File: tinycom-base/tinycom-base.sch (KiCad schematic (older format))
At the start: 34 parts, among them J1 MICRO_SD_HINGE, P1 CONN_02X08, P2 CONN_02X08, P3 USB_A, P4 USB_OTG, U1 SY8008BAAC, U2 SY8008BAAC, U3 SY8008BAAC

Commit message: rename wifi->basse
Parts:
- removed R10, R11, R12, R8, R9: R_Small, Resistors_SMD:R_0805, symbol R_Small
- added HDMI1: HDMI-SWM-19, tinycom:HDMI-SWM-19, symbol HDMI-SWM-19
- added U4: RTL8723BS(ComboModule), tinycom:RL-SM02BD(RTL8723BS), symbol RTL8723BS(ComboModule)
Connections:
- wire segments 124 -> 118
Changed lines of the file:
@@
 LIBS:stm32-48pin-devBoard
 LIBS:OPL-Inductor
-LIBS:tinycom-base-cache
+LIBS:tinycom
+LIBS:hdmi-swm-19
+LIBS:tinycom-wifi-cache
 EELAYER 25 0
 EELAYER END
@@
 $EndComp
 $Comp
-L MICRO_SD_HINGE J1
-U 1 1 562BAACC
-P 8950 4450
-F 0 "J1" H 9000 4500 60  0000 C CNN
-F 1 "MICRO_SD_HINGE" H 8950 5000 60  0000 C CNN
-F 2 "armory:MICRO_SD_HINGE_AMP" V 9060 3950 60  0001 C CNN
-F 3 "" V 9060 3950 60  0000 C CNN
-	1    8950 4450
-	1    0    0    -1
-$EndComp
-$Comp
 L SY8008BAAC U1
 U 1 1 562D9C58
@@
 $EndComp
 $Comp
-L +5V #PWR01
+L +5V #PWR14
 U 1 1 562DA8F7
 P 5250 4200
-F 0 "#PWR01" H 5250 4050 50  0001 C CNN
+F 0 "#PWR14" H 5250 4050 50  0001 C CNN
 F 1 "+5V" H 5250 4340 50  0000 C CNN
 F 2 "" H 5250 4200 60  0000 C CNN
@@
 $EndComp
 $Comp
-L GND #PWR02
+L GND #PWR15
 U 1 1 562DA928
 P 5250 4600
-F 0 "#PWR02" H 5250 4350 50  0001 C CNN
+F 0 "#PWR15" H 5250 4350 50  0001 C CNN
 F 1 "GND" H 5250 4450 50  0000 C CNN
 F 2 "" H 5250 4600 60  0000 C CNN
@@
 UDP0
 $Comp
-L +5V #PWR03
+L +5V #PWR16
 U 1 1 562DAC42
 P 5300 5050
-F 0 "#PWR03" H 5300 4900 50  0001 C CNN
+F 0 "#PWR16" H 5300 4900 50  0001 C CNN
 F 1 "+5V" H 5300 5190 50  0000 C CNN
 F 2 "" H 5300 5050 60  0000 C CNN
@@
 $EndComp
 $Comp
-L GND #PWR04
+L GND #PWR17
 U 1 1 562DAC77
 P 5300 5500
-F 0 "#PWR04" H 5300 5250 50  0001 C CNN
+F 0 "#PWR17" H 5300 5250 50  0001 C CNN
 F 1 "GND" H 5300 5350 50  0000 C CNN
 F 2 "" H 5300 5500 60  0000 C CNN
@@
 UDP1
 $Comp
-L GND #PWR05
+L GND #PWR5
 U 1 1 562DAF0B
 P 1350 1750
-F 0 "#PWR05" H 1350 1500 50  0001 C CNN
+F 0 "#PWR5" H 1350 1500 50  0001 C CNN
 F 1 "GND" H 1350 1600 50  0000 C CNN
 F 2 "" H 1350 1750 60  0000 C CNN
@@
 $EndComp
 $Comp
-L +5V #PWR06
+L +5V #PWR3
 U 1 1 562DAF87
 P 1250 1350
-F 0 "#PWR06" H 1250 1200 50  0001 C CNN
+F 0 "#PWR3" H 1250 1200 50  0001 C CNN
 F 1 "+5V" H 1250 1490 50  0000 C CNN
 F 2 "" H 1250 1350 60  0000 C CNN
@@
 $EndComp
 $Comp
-L +5V #PWR07
+L +5V #PWR1
 U 1 1 562DB0A5
 P 1150 2550
-F 0 "#PWR07" H 1150 2400 50  0001 C CNN
+F 0 "#PWR1" H 1150 2400 50  0001 C CNN
 F 1 "+5V" H 1150 2690 50  0000 C CNN
 F 2 "" H 1150 2550 60  0000 C CNN
@@
 $EndComp
 $Comp
-L GND #PWR08
+L GND #PWR6
 U 1 1 562DB1B7
 P 1350 2900
-F 0 "#PWR08" H 1350 2650 50  0001 C CNN
+F 0 "#PWR6" H 1350 2650 50  0001 C CNN
 F 1 "GND" H 1350 2750 50  0000 C CNN
 F 2 "" H 1350 2900 60  0000 C CNN
@@
 $EndComp
 $Comp
-L +5V #PWR09
+L +5V #PWR2
 U 1 1 562DB2B7
 P 1150 3800
-F 0 "#PWR09" H 1150 3650 50  0001 C CNN
+F 0 "#PWR2" H 1150 3650 50  0001 C CNN
 F 1 "+5V" H 1150 3940 50  0000 C CNN
 F 2 "" H 1150 3800 60  0000 C CNN
@@
 $EndComp
 $Comp
-L GND #PWR010
+L GND #PWR4
 U 1 1 562DB346
 P 1300 4150
-F 0 "#PWR010" H 1300 3900 50  0001 C CNN
+F 0 "#PWR4" H 1300 3900 50  0001 C CNN
 F 1 "GND" H 1300 4000 50  0000 C CNN
 F 2 "" H 1300 4150 60  0000 C CNN
@@
 VCC_15
 $Comp
-L GND #PWR011
+L GND #PWR19
 U 1 1 562DAEC4
 P 7450 2400
-F 0 "#PWR011" H 7450 2150 50  0001 C CNN
+F 0 "#PWR19" H 7450 2150 50  0001 C CNN
 F 1 "GND" H 7450 2250 50  0000 C CNN
 F 2 "" H 7450 2400 60  0000 C CNN
@@
 $EndComp
 $Comp
-L GND #PWR012
+L GND #PWR21
 U 1 1 562DA997
 P 8650 2450
-F 0 "#PWR012" H 8650 2200 50  0001 C CNN
+F 0 "#PWR21" H 8650 2200 50  0001 C CNN
 F 1 "GND" H 8650 2300 50  0000 C CNN
 F 2 "" H 8650 2450 60  0000 C CNN
@@
 SDC0_D1
 $Comp
-L GND #PWR013
+L GND #PWR20
 U 1 1 562DAEE9
 P 7450 4950
-F 0 "#PWR013" H 7450 4700 50  0001 C CNN
+F 0 "#PWR20" H 7450 4700 50  0001 C CNN
 F 1 "GND" H 7450 4800 50  0000 C CNN
 F 2 "" H 7450 4950 60  0000 C CNN
@@
 $EndComp
 $Comp
-L GND #PWR014
+L GND #PWR22
 U 1 1 562DAF47
 P 9050 5450
-F 0 "#PWR014" H 9050 5200 50  0001 C CNN
+F 0 "#PWR22" H 9050 5200 50  0001 C CNN
 F 1 "GND" H 9050 5300 50  0000 C CNN
 F 2 "" H 9050 5450 60  0000 C CNN
@@
 $EndComp
 $Comp
-L +3.3V #PWR015
+L +3.3V #PWR18
 U 1 1 562DB369
 P 7300 4000
-F 0 "#PWR015" H 7300 3850 50  0001 C CNN
+F 0 "#PWR18" H 7300 3850 50  0001 C CNN
 F 1 "+3.3V" H 7300 4140 50  0000 C CNN
 F 2 "" H 7300 4000 60  0000 C CNN
@@
 $EndComp
 $Comp
-L GND #PWR016
+L GND #PWR9
 U 1 1 562DB89F
 P 3250 2000
-F 0 "#PWR016" H 3250 1750 50  0001 C CNN
+F 0 "#PWR9" H 3250 1750 50  0001 C CNN
 F 1 "GND" H 3250 1850 50  0000 C CNN
 F 2 "" H 3250 2000 60  0000 C CNN
@@
 $EndComp
 $Comp
-L +3.3V #PWR017
+L +3.3V #PWR10
 U 1 1 562DBC47
 P 3600 1350
-F 0 "#PWR017" H 3600 1200 50  0001 C CNN
+F 0 "#PWR10" H 3600 1200 50  0001 C CNN
 F 1 "+3.3V" H 3600 1490 50  0000 C CNN
 F 2 "" H 3600 1350 60  0000 C CNN
@@
 $EndComp
 $Comp
-L GND #PWR018
+L GND #PWR8
 U 1 1 562F8BF0
 P 3150 3150
-F 0 "#PWR018" H 3150 2900 50  0001 C CNN
+F 0 "#PWR8" H 3150 2900 50  0001 C CNN
 F 1 "GND" H 3150 3000 50  0000 C CNN
 F 2 "" H 3150 3150 60  0000 C CNN
@@
 $EndComp
 $Comp
-L GND #PWR019
+L GND #PWR7
 U 1 1 562F9FD4
 P 3100 4550
-F 0 "#PWR019" H 3100 4300 50  0001 C CNN
+F 0 "#PWR7" H 3100 4300 50  0001 C CNN
 F 1 "GND" H 3100 4400 50  0000 C CNN
 F 2 "" H 3100 4550 60  0000 C CNN
@@
 $EndComp
 $Comp
-L GND #PWR020
+L GND #PWR11
 U 1 1 56336272
 P 4400 1900
-F 0 "#PWR020" H 4400 1650 50  0001 C CNN
+F 0 "#PWR11" H 4400 1650 50  0001 C CNN
 F 1 "GND" H 4400 1750 50  0000 C CNN
 F 2 "" H 4400 1900 60  0000 C CNN
@@
 $EndComp
 $Comp
-L +3.3V #PWR021
-U 1 1 563494F9
-P 8050 3600
-F 0 "#PWR021" H 8050 3450 50  0001 C CNN
-F 1 "+3.3V" H 8050 3740 50  0000 C CNN
-F 2 "" H 8050 3600 60  0000 C CNN
-F 3 "" H 8050 3600 60  0000 C CNN
-	1    8050 3600
-	1    0    0    -1
-$EndComp
-$Comp
-L R_Small R8
-U 1 1 56349670
-P 7850 3750
-F 0 "R8" H 7880 3770 50  0000 L CNN
-F 1 "R_Small" H 7880 3710 50  0000 L CNN
-F 2 "Resistors_SMD:R_0805" H 7850 3750 60  0001 C CNN
-F 3 "" H 7850 3750 60  0000 C CNN
-	1    7850 3750
-	1    0    0    -1
-$EndComp
-$Comp
-L R_Small R9
-U 1 1 56349787
-P 7950 3750
-F 0 "R9" H 7980 3770 50  0000 L CNN
-F 1 "R_Small" H 7980 3710 50  0000 L CNN
-F 2 "Resistors_SMD:R_0805" H 7950 3750 60  0001 C CNN
-F 3 "" H 7950 3750 60  0000 C CNN
-	1    7950 3750
-	1    0    0    -1
-$EndComp
-$Comp
-L R_Small R10
-U 1 1 56349823
-P 8050 3750
-F 0 "R10" H 8080 3770 50  0000 L CNN
-F 1 "R_Small" H 8080 3710 50  0000 L CNN
-F 2 "Resistors_SMD:R_0805" H 8050 3750 60  0001 C CNN
-F 3 "" H 8050 3750 60  0000 C CNN
-	1    8050 3750
-	1    0    0    -1
-$EndComp
-$Comp
-L R_Small R11
-U 1 1 5634988E
-P 8150 3750
-F 0 "R11" H 8180 3770 50  0000 L CNN
-F 1 "R_Small" H 8180 3710 50  0000 L CNN
-F 2 "Resistors_SMD:R_0805" H 8150 3750 60  0001 C CNN
-F 3 "" H 8150 3750 60  0000 C CNN
-	1    8150 3750
-	1    0    0    -1
-$EndComp
-$Comp
-L R_Small R12
-U 1 1 56349916
-P 8250 3750
-F 0 "R12" H 8280 3770 50  0000 L CNN
-F 1 "R_Small" H 8280 3710 50  0000 L CNN
-F 2 "Resistors_SMD:R_0805" H 8250 3750 60  0001 C CNN
-F 3 "" H 8250 3750 60  0000 C CNN
-	1    8250 3750
-	1    0    0    -1
-$EndComp
-$Comp
 L C_Small C8
 U 1 1 5634A812
@@
 $EndComp
 $Comp
-L GND #PWR022
+L GND #PWR12
 U 1 1 5634B03F
 P 4900 4550
-F 0 "#PWR022" H 4900 4300 50  0001 C CNN
+F 0 "#PWR12" H 4900 4300 50  0001 C CNN
 F 1 "GND" H 4900 4400 50  0000 C CNN
 F 2 "" H 4900 4550 60  0000 C CNN
@@
 $EndComp
 $Comp
-L GND #PWR023
+L GND #PWR13
 U 1 1 5634B0B0
 P 4900 5400
-F 0 "#PWR023" H 4900 5150 50  0001 C CNN
+F 0 "#PWR13" H 4900 5150 50  0001 C CNN
 F 1 "GND" H 4900 5250 50  0000 C CNN
 F 2 "" H 4900 5400 60  0000 C CNN
@@
 	8150 4050 7900 4050
 Wire Wire Line
-	7850 3600 8250 3600
-Wire Wire Line
-	7850 3600 7850 3650
-Wire Wire Line
-	8250 3600 8250 3650
-Connection ~ 8050 3600
-Wire Wire Line
-	7950 3650 7950 3600
-Connection ~ 7950 3600
-Wire Wire Line
-	8050 3650 8050 3600
-Wire Wire Line
-	8150 3650 8150 3600
-Connection ~ 8150 3600
-Wire Wire Line
-	8250 3850 8250 4000
-Wire Wire Line
 	8250 4000 8150 4000
 Wire Wire Line
 	8150 4000 8150 4050
-Wire Wire Line
-	8150 3850 8150 3900
-Wire Wire Line
-	8150 3900 8100 3900
-Wire Wire Line
-	8100 3900 8100 4150
 Connection ~ 8100 4150
-Wire Wire Line
-	8050 3850 8050 4250
 Connection ~ 8050 4250
-Wire Wire Line
-	8000 4650 8000 3850
-Wire Wire Line
-	8000 3850 7950 3850
 Connection ~ 8000 4650
-Wire Wire Line
-	7850 3850 7850 3950
-Wire Wire Line
-	7850 3950 7950 3950
-Wire Wire Line
-	7950 3950 7950 4750
 Connection ~ 7950 4750
 Wire Wire Line
@@
 	5350 4850 5850 4850
 Connection ~ 5350 4650
+$Comp
+L RTL8723BS(ComboModule) U4
+U 1 1 56591901
+P 2000 6200
+F 0 "U4" H 1600 7575 60  0000 C CNN
+F 1 "RTL8723BS(ComboModule)" H 2000 4825 60  0000 C CNN
+F 2 "tinycom:RL-SM02BD(RTL8723BS)" H 2000 6000 60  0000 C CNN
+F 3 "" H 2000 6000 60  0000 C CNN
+	1    2000 6200
+	1    0    0    -1
+$EndComp
+Wire Wire Line
+	7950 3950 7950 4750
+Wire Wire Line
+	7850 3950 7950 3950
+Wire Wire Line
+	7850 3850 7850 3950
+Wire Wire Line
+	8000 3850 7950 3850
+Wire Wire Line
+	8000 4650 8000 3850
+Wire Wire Line
+	8050 3850 8050 4250
+Wire Wire Line
+	8100 3900 8100 4150
+Wire Wire Line
+	8150 3900 8100 3900
+Wire Wire Line
+	8150 3850 8150 3900
+$Comp
+L MICRO_SD_HINGE J1
+U 1 1 562BAACC
+P 8950 4450
+F 0 "J1" H 9000 4500 60  0000 C CNN
+F 1 "MICRO_SD_HINGE" H 8950 5000 60  0000 C CNN
+F 2 "armory:MICRO_SD_HINGE_AMP" V 9060 3950 60  0001 C CNN
+F 3 "" V 9060 3950 60  0000 C CNN
+	1    8950 4450
+	1    0    0    -1
+$EndComp
+Wire Wire Line
+	8250 3850 8250 4000
+$Comp
+L HDMI-SWM-19 HDMI1
+U 1 1 56591D96
+P 3450 6150
+F 0 "HDMI1" H 3550 7150 50  0000 L BNN
+F 1 "HDMI-SWM-19" H 3550 5050 50  0000 L BNN
+F 2 "tinycom:HDMI-SWM-19" H 3480 6300 20  0001 C CNN
+F 3 "" H 3450 6150 60  0000 C CNN
+	1    3450 6150
+	1    0    0    -1
+$EndComp
 $EndSCHEMATC

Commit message: improve base board
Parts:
- removed P1, P2: CONN_02X08, Socket_Strips:Socket_Strip_Straight_2x08, symbol CONN_02X08
- removed U4: RTL8723BS(ComboModule), tinycom:RL-SM02BD(RTL8723BS), symbol RTL8723BS(ComboModule)
- added P1, P2: CONN_02X10, Socket_Strips:Socket_Strip_Straight_2x10, symbol CONN_02X10
- added U4: RTL8188, tinycom:RTL8188, symbol RTL8188
- added U5: rainsun-antenna, tinycom:rainsun-antenna, symbol rainsun-antenna
- added U?: sata-smd, Connect:SATA-7_SMD, symbol sata-smd
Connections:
- net labels added: HCEC, HCSL, HHPD, HSDA, HTX0N, HTX0P, HTX1N, HTX1P, HTX2N, HTX2P, HTXCN, HTXCP, MIC, SATA_RXM, SATA_RXP, SATA_TXM, SATA_TXP, UART0_RX, UART0_TX, UDM2, UDP2, VCC_12, VCC_25
- wire segments 118 -> 132
- no-connect marks 16 -> 0

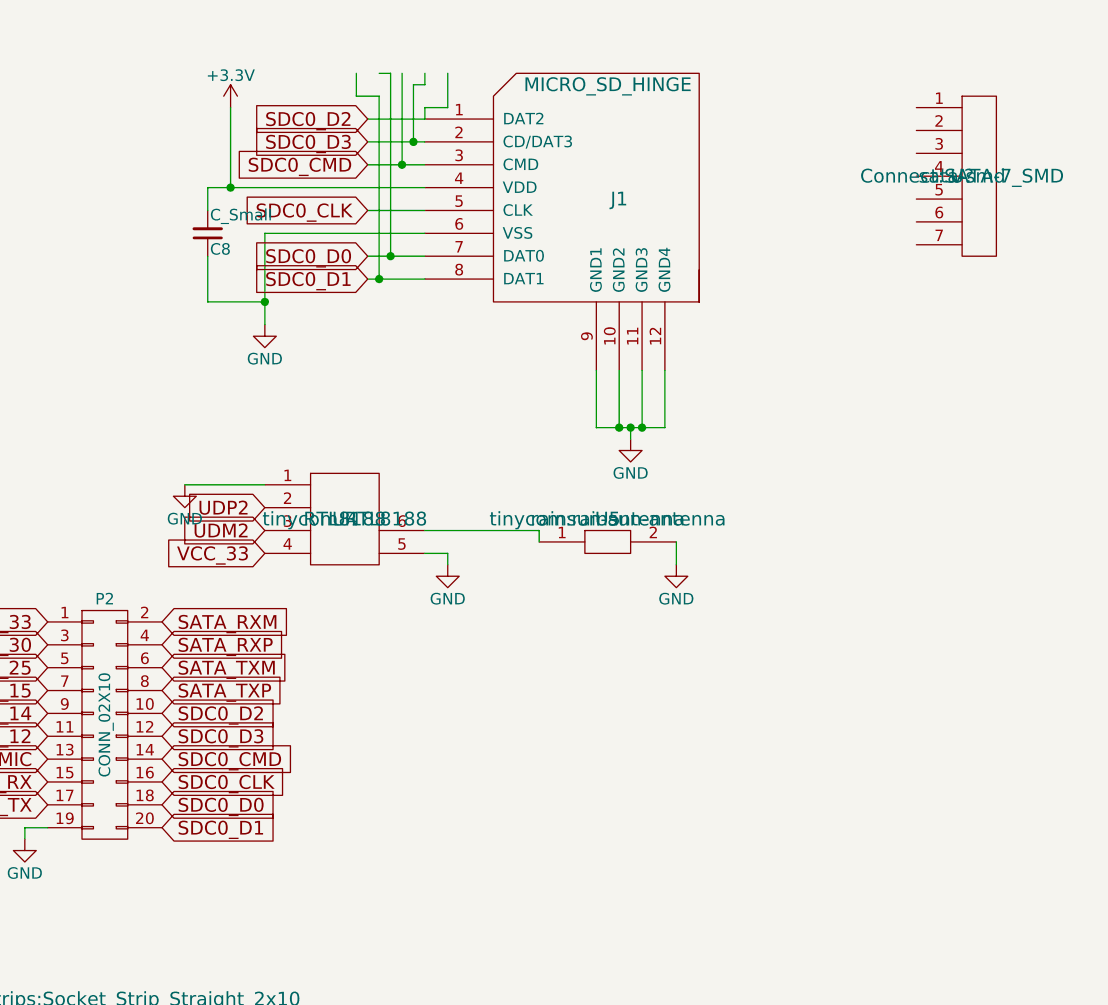
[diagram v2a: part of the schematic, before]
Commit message: move sata
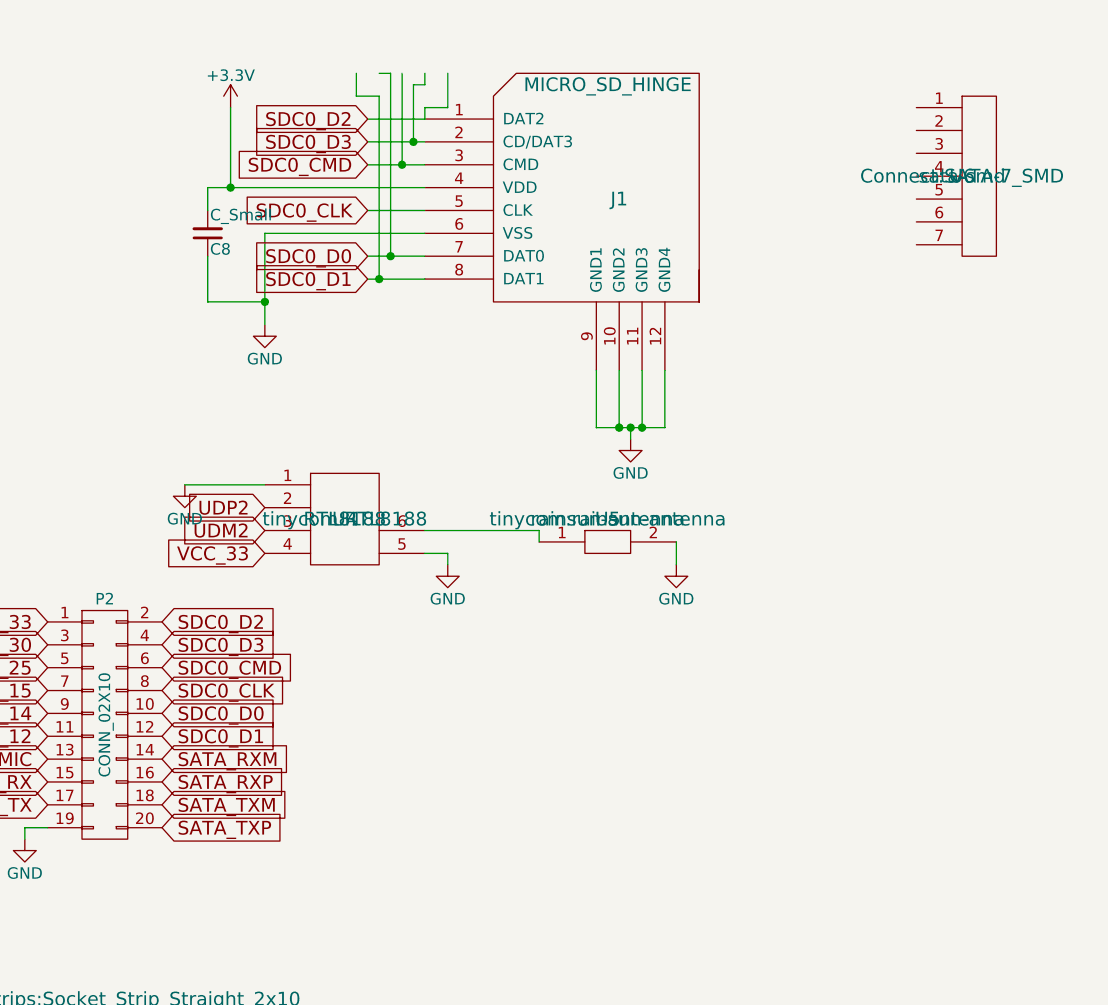
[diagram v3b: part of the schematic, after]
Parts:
- gave numbers to parts that had none: 1
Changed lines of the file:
@@
 $EndComp
 $Comp
-L +5V #PWR01
+L +5V #PWR16
 U 1 1 562DA8F7
 P 5250 4200
-F 0 "#PWR01" H 5250 4050 50  0001 C CNN
+F 0 "#PWR16" H 5250 4050 50  0001 C CNN
 F 1 "+5V" H 5250 4340 50  0000 C CNN
 F 2 "" H 5250 4200 60  0000 C CNN
@@
 $EndComp
 $Comp
-L GND #PWR02
+L GND #PWR17
 U 1 1 562DA928
 P 5250 4600
-F 0 "#PWR02" H 5250 4350 50  0001 C CNN
+F 0 "#PWR17" H 5250 4350 50  0001 C CNN
 F 1 "GND" H 5250 4450 50  0000 C CNN
 F 2 "" H 5250 4600 60  0000 C CNN
@@
 UDP0
 $Comp
-L +5V #PWR03
+L +5V #PWR18
 U 1 1 562DAC42
 P 5300 5050
-F 0 "#PWR03" H 5300 4900 50  0001 C CNN
+F 0 "#PWR18" H 5300 4900 50  0001 C CNN
 F 1 "+5V" H 5300 5190 50  0000 C CNN
 F 2 "" H 5300 5050 60  0000 C CNN
@@
 $EndComp
 $Comp
-L GND #PWR04
+L GND #PWR19
 U 1 1 562DAC77
 P 5300 5500
-F 0 "#PWR04" H 5300 5250 50  0001 C CNN
+F 0 "#PWR19" H 5300 5250 50  0001 C CNN
 F 1 "GND" H 5300 5350 50  0000 C CNN
 F 2 "" H 5300 5500 60  0000 C CNN
@@
 UDP1
 $Comp
-L GND #PWR05
+L GND #PWR5
 U 1 1 562DAF0B
 P 1350 1750
-F 0 "#PWR05" H 1350 1500 50  0001 C CNN
+F 0 "#PWR5" H 1350 1500 50  0001 C CNN
 F 1 "GND" H 1350 1600 50  0000 C CNN
 F 2 "" H 1350 1750 60  0000 C CNN
@@
 $EndComp
 $Comp
-L +5V #PWR06
+L +5V #PWR3
 U 1 1 562DAF87
 P 1250 1350
-F 0 "#PWR06" H 1250 1200 50  0001 C CNN
+F 0 "#PWR3" H 1250 1200 50  0001 C CNN
 F 1 "+5V" H 1250 1490 50  0000 C CNN
 F 2 "" H 1250 1350 60  0000 C CNN
@@
 $EndComp
 $Comp
-L +5V #PWR07
+L +5V #PWR1
 U 1 1 562DB0A5
 P 1150 2550
-F 0 "#PWR07" H 1150 2400 50  0001 C CNN
+F 0 "#PWR1" H 1150 2400 50  0001 C CNN
 F 1 "+5V" H 1150 2690 50  0000 C CNN
 F 2 "" H 1150 2550 60  0000 C CNN
@@
 $EndComp
 $Comp
-L GND #PWR08
+L GND #PWR6
 U 1 1 562DB1B7
 P 1350 2900
-F 0 "#PWR08" H 1350 2650 50  0001 C CNN
+F 0 "#PWR6" H 1350 2650 50  0001 C CNN
 F 1 "GND" H 1350 2750 50  0000 C CNN
 F 2 "" H 1350 2900 60  0000 C CNN
@@
 $EndComp
 $Comp
-L +5V #PWR09
+L +5V #PWR2
 U 1 1 562DB2B7
 P 1150 3800
-F 0 "#PWR09" H 1150 3650 50  0001 C CNN
+F 0 "#PWR2" H 1150 3650 50  0001 C CNN
 F 1 "+5V" H 1150 3940 50  0000 C CNN
 F 2 "" H 1150 3800 60  0000 C CNN
@@
 $EndComp
 $Comp
-L GND #PWR010
+L GND #PWR4
 U 1 1 562DB346
 P 1300 4150
-F 0 "#PWR010" H 1300 3900 50  0001 C CNN
+F 0 "#PWR4" H 1300 3900 50  0001 C CNN
 F 1 "GND" H 1300 4000 50  0000 C CNN
 F 2 "" H 1300 4150 60  0000 C CNN
@@
 UDP1
 $Comp
-L GND #PWR011
+L GND #PWR20
 U 1 1 562DAEC4
 P 5800 6000
-F 0 "#PWR011" H 5800 5750 50  0001 C CNN
+F 0 "#PWR20" H 5800 5750 50  0001 C CNN
 F 1 "GND" H 5800 5850 50  0000 C CNN
 F 2 "" H 5800 6000 60  0000 C CNN
@@
 $EndComp
 $Comp
-L GND #PWR012
+L GND #PWR21
 U 1 1 562DA997
 P 6400 7200
-F 0 "#PWR012" H 6400 6950 50  0001 C CNN
+F 0 "#PWR21" H 6400 6950 50  0001 C CNN
 F 1 "GND" H 6400 7050 50  0000 C CNN
 F 2 "" H 6400 7200 60  0000 C CNN
@@
 SDC0_D1
 $Comp
-L GND #PWR013
+L GND #PWR24
 U 1 1 562DAEE9
 P 7450 4950
-F 0 "#PWR013" H 7450 4700 50  0001 C CNN
+F 0 "#PWR24" H 7450 4700 50  0001 C CNN
 F 1 "GND" H 7450 4800 50  0000 C CNN
 F 2 "" H 7450 4950 60  0000 C CNN
@@
 $EndComp
 $Comp
-L GND #PWR014
+L GND #PWR26
 U 1 1 562DAF47
 P 9050 5450
-F 0 "#PWR014" H 9050 5200 50  0001 C CNN
+F 0 "#PWR26" H 9050 5200 50  0001 C CNN
 F 1 "GND" H 9050 5300 50  0000 C CNN
 F 2 "" H 9050 5450 60  0000 C CNN
@@
 $EndComp
 $Comp
-L +3.3V #PWR015
+L +3.3V #PWR23
 U 1 1 562DB369
 P 7300 4000
-F 0 "#PWR015" H 7300 3850 50  0001 C CNN
+F 0 "#PWR23" H 7300 3850 50  0001 C CNN
 F 1 "+3.3V" H 7300 4140 50  0000 C CNN
 F 2 "" H 7300 4000 60  0000 C CNN
@@
 $EndComp
 $Comp
-L GND #PWR016
+L GND #PWR9
 U 1 1 562DB89F
 P 3250 2000
-F 0 "#PWR016" H 3250 1750 50  0001 C CNN
+F 0 "#PWR9" H 3250 1750 50  0001 C CNN
 F 1 "GND" H 3250 1850 50  0000 C CNN
 F 2 "" H 3250 2000 60  0000 C CNN
@@
 $EndComp
 $Comp
-L +3.3V #PWR017
+L +3.3V #PWR10
 U 1 1 562DBC47
 P 3600 1350
-F 0 "#PWR017" H 3600 1200 50  0001 C CNN
+F 0 "#PWR10" H 3600 1200 50  0001 C CNN
 F 1 "+3.3V" H 3600 1490 50  0000 C CNN
 F 2 "" H 3600 1350 60  0000 C CNN
@@
 $EndComp
 $Comp
-L GND #PWR018
+L GND #PWR8
 U 1 1 562F8BF0
 P 3150 3150
-F 0 "#PWR018" H 3150 2900 50  0001 C CNN
+F 0 "#PWR8" H 3150 2900 50  0001 C CNN
 F 1 "GND" H 3150 3000 50  0000 C CNN
 F 2 "" H 3150 3150 60  0000 C CNN
@@
 $EndComp
 $Comp
-L GND #PWR019
+L GND #PWR7
 U 1 1 562F9FD4
 P 3100 4550
-F 0 "#PWR019" H 3100 4300 50  0001 C CNN
+F 0 "#PWR7" H 3100 4300 50  0001 C CNN
 F 1 "GND" H 3100 4400 50  0000 C CNN
 F 2 "" H 3100 4550 60  0000 C CNN
@@
 $EndComp
 $Comp
-L GND #PWR020
+L GND #PWR12
 U 1 1 56336272
 P 4400 1900
-F 0 "#PWR020" H 4400 1650 50  0001 C CNN
+F 0 "#PWR12" H 4400 1650 50  0001 C CNN
 F 1 "GND" H 4400 1750 50  0000 C CNN
 F 2 "" H 4400 1900 60  0000 C CNN
@@
 $EndComp
 $Comp
-L GND #PWR021
+L GND #PWR14
 U 1 1 5634B03F
 P 4900 4550
-F 0 "#PWR021" H 4900 4300 50  0001 C CNN
+F 0 "#PWR14" H 4900 4300 50  0001 C CNN
 F 1 "GND" H 4900 4400 50  0000 C CNN
 F 2 "" H 4900 4550 60  0000 C CNN
@@
 $EndComp
 $Comp
-L GND #PWR022
+L GND #PWR15
 U 1 1 5634B0B0
 P 4900 5400
-F 0 "#PWR022" H 4900 5150 50  0001 C CNN
+F 0 "#PWR15" H 4900 5150 50  0001 C CNN
 F 1 "GND" H 4900 5250 50  0000 C CNN
 F 2 "" H 4900 5400 60  0000 C CNN
@@
 HHPD
 $Comp
-L GND #PWR023
+L GND #PWR11
 U 1 1 5659A9B5
 P 4250 7400
-F 0 "#PWR023" H 4250 7150 50  0001 C CNN
+F 0 "#PWR11" H 4250 7150 50  0001 C CNN
 F 1 "GND" H 4250 7250 50  0000 C CNN
 F 2 "" H 4250 7400 60  0000 C CNN
@@
 Connection ~ 4250 6850
 $Comp
-L +5V #PWR024
+L +5V #PWR13
 U 1 1 5659B3AA
 P 4550 6900
-F 0 "#PWR024" H 4550 6750 50  0001 C CNN
+F 0 "#PWR13" H 4550 6750 50  0001 C CNN
 F 1 "+5V" H 4550 7040 50  0000 C CNN
 F 2 "" H 4550 6900 60  0000 C CNN
@@
 $EndComp
 $Comp
-L GND #PWR025
+L GND #PWR25
 U 1 1 565A1BF7
 P 8250 6000
-F 0 "#PWR025" H 8250 5750 50  0001 C CNN
+F 0 "#PWR25" H 8250 5750 50  0001 C CNN
 F 1 "GND" H 8250 5850 50  0000 C CNN
 F 2 "" H 8250 6000 60  0000 C CNN
@@
 	8250 5950 8250 6000
 $Comp
-L GND #PWR026
+L GND #PWR22
 U 1 1 565A1DA6
 P 7100 5650
-F 0 "#PWR026" H 7100 5400 50  0001 C CNN
+F 0 "#PWR22" H 7100 5400 50  0001 C CNN
 F 1 "GND" H 7100 5500 50  0000 C CNN
 F 2 "" H 7100 5650 60  0000 C CNN
@@
 Text GLabel 7450 5950 0    60   Input ~ 0
 VCC_33
-Text GLabel 7000 7150 2    60   Input ~ 0
+Text GLabel 7000 6750 2    60   Input ~ 0
 SDC0_D1
 $Comp
@@
 	1    0    0    -1
 $EndComp
-Text GLabel 7000 7050 2    60   Input ~ 0
+Text GLabel 7000 6650 2    60   Input ~ 0
 SDC0_D0
-Text GLabel 7000 6950 2    60   Input ~ 0
+Text GLabel 7000 6550 2    60   Input ~ 0
 SDC0_CLK
-Text GLabel 7000 6850 2    60   Input ~ 0
+Text GLabel 7000 6450 2    60   Input ~ 0
 SDC0_CMD
-Text GLabel 7000 6750 2    60   Input ~ 0
+Text GLabel 7000 6350 2    60   Input ~ 0
 SDC0_D3
-Text GLabel 7000 6650 2    60   Input ~ 0
+Text GLabel 7000 6250 2    60   Input ~ 0
 SDC0_D2
 Text GLabel 5650 6350 2    60   Input ~ 0
@@
 	8650 5850 8650 5900
 $Comp
-L GND #PWR027
+L GND #PWR27
 U 1 1 565A4582
 P 9250 6000
-F 0 "#PWR027" H 9250 5750 50  0001 C CNN
+F 0 "#PWR27" H 9250 5750 50  0001 C CNN
 F 1 "GND" H 9250 5850 50  0000 C CNN
 F 2 "" H 9250 6000 60  0000 C CNN
@@
 Text GLabel 6500 6950 0    60   Input ~ 0
 UART0_RX
-Text GLabel 7000 6550 2    60   Input ~ 0
+Text GLabel 7000 7150 2    60   Input ~ 0
 SATA_TXP
-Text GLabel 7000 6450 2    60   Input ~ 0
+Text GLabel 7000 7050 2    60   Input ~ 0
 SATA_TXM
-Text GLabel 7000 6350 2    60   Input ~ 0
+Text GLabel 7000 6950 2    60   Input ~ 0
 SATA_RXP
-Text GLabel 7000 6250 2    60   Input ~ 0
+Text GLabel 7000 6850 2    60   Input ~ 0
 SATA_RXM
 Text GLabel 6500 6750 0    60   Input ~ 0
@@
 	6400 7150 6400 7200
 $Comp
-L sata-smd U?
+L sata-smd U6
 U 1 1 5659F5B9
 P 10500 4300
-F 0 "U?" H 10500 4300 60  0000 C CNN
+F 0 "U6" H 10500 4300 60  0000 C CNN
 F 1 "sata-smd" H 10500 4300 60  0000 C CNN
 F 2 "Connect:SATA-7_SMD" H 10500 4300 60  0000 C CNN
